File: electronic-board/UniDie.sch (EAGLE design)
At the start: 24 parts, among them IC1 ATMEGA88-THIN

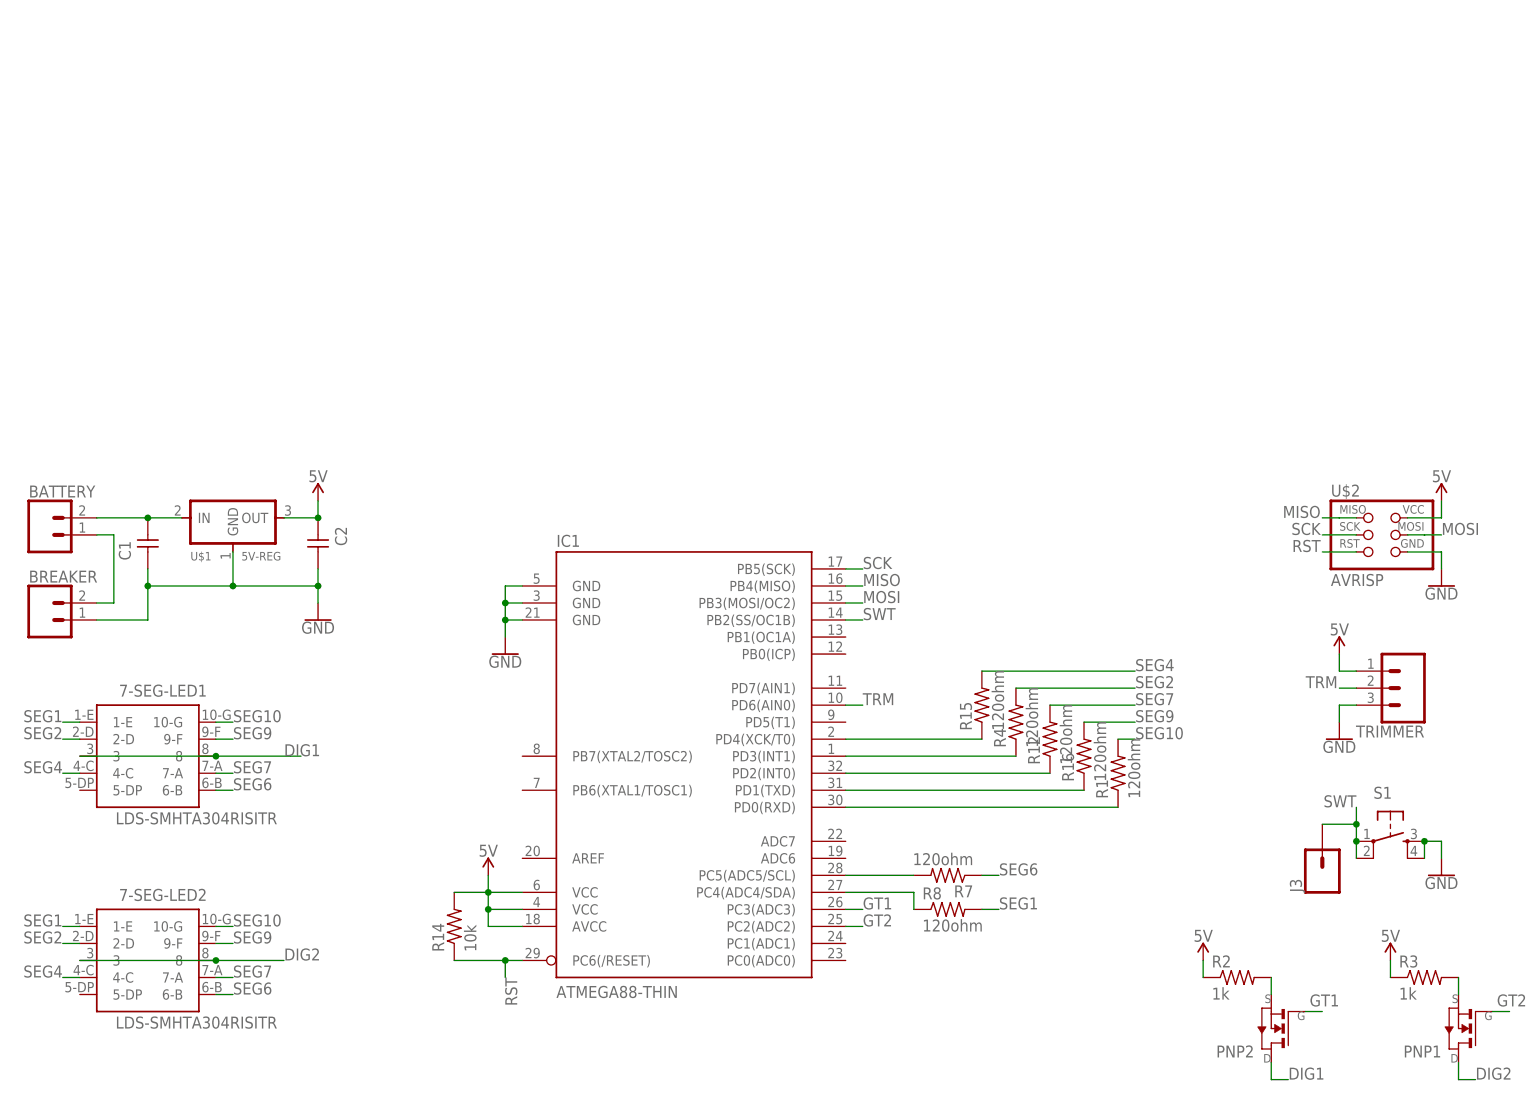
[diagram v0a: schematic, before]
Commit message: Design schematics for new controller
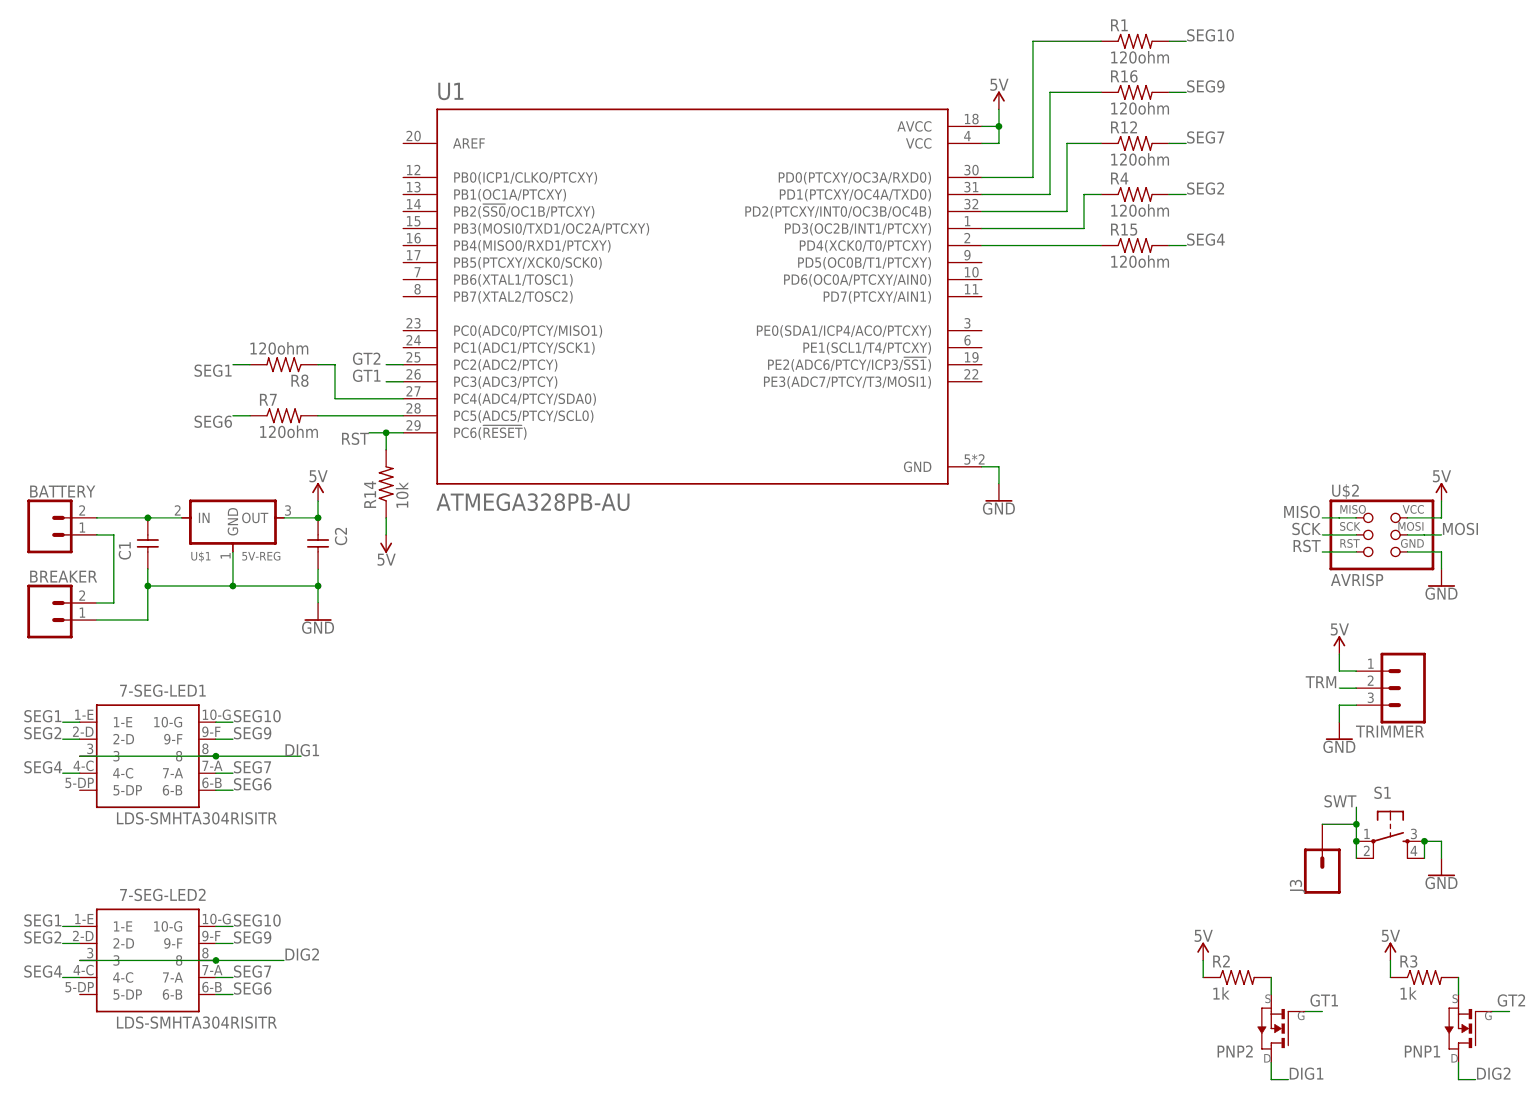
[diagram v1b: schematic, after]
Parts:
- removed IC1: ATMEGA88-THIN, fab:ATMEGA88-THIN
- added U1: ATMEGA328PB-AU, ATMEGA328PB-AU:ATMEGA328PB-AU
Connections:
- net 5V: now also R14.1, U1.AVCC, U1.VCC; no longer IC1.AVCC, IC1.VCC@1, IC1.VCC@2, R14.2
- net GND: now also U1.GND; no longer IC1.GND, IC1.GND@1, IC1.GND@2
- net GT1: now also U1.PC3(ADC3/PTCY); no longer IC1.PC3(ADC3)
- net GT2: now also U1.PC2(ADC2/PTCY); no longer IC1.PC2(ADC2)
- net MISO: no longer IC1.PB4(MISO)
- net MOSI: no longer IC1.PB3(MOSI/OC2)
- net N$10: now also U1.PD0(PTCXY/OC3A/RXD0); no longer IC1.PD0(RXD)
- net N$3: now also U1.PC5(ADC5/PTCY/SCL0); no longer IC1.PC5(ADC5/SCL)
- net N$4: now also U1.PC4(ADC4/PTCY/SDA0); no longer IC1.PC4(ADC4/SDA)
- net N$6: now also U1.PD4(XCK0/T0/PTCXY); no longer IC1.PD4(XCK/T0)
- net N$7: now also U1.PD3(OC2B/INT1/PTCXY); no longer IC1.PD3(INT1)
- net N$8: now also U1.PD2(PTCXY/INT0/OC3B/OC4B); no longer IC1.PD2(INT0)
- net N$9: now also U1.PD1(PTCXY/OC4A/TXD0); no longer IC1.PD1(TXD)
- net RST: now also R14.2, U1.PC6(!RESET!); no longer IC1.PC6(/RESET), R14.1
- net SCK: no longer IC1.PB5(SCK)
- net SWT: no longer IC1.PB2(SS/OC1B)
- net TRM: no longer IC1.PD6(AIN0)
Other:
- moved on the sheet: R1, R12, R14, R15, R16, R4, R7, R8

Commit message: Add thinner traces package for the microcontroller, re-arrange routes. To be finishes
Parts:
- removed U1: ATMEGA328PB-AU, ATMEGA328PB-AU:ATMEGA328PB-AU
- added U$3: ATMEGA328PB-AU-THIN, AG:ATMEGA328PB-AU-THIN
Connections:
- net 5V: now also U$3.AVCC, U$3.VCC; no longer U1.AVCC, U1.VCC
- net GND: now also U$3.GND, U$3.GND@1; no longer U1.GND
- net GT1: now also U$3.PC3(ADC3/PTCY); no longer U1.PC3(ADC3/PTCY)
- net GT2: now also U$3.PC2(ADC2/PTCY); no longer U1.PC2(ADC2/PTCY)
- net MISO: now also U$3.PC0(ADC0/PTCY/MISO1)
- net MOSI: now also U$3.PE3(ADC7/PTCY/T3/MOSI1)
- net N$10: now also U$3.PD0(PTCXY/OC3A/RXD0); no longer U1.PD0(PTCXY/OC3A/RXD0)
- net N$3: now also U$3.PC5(ADC5/PTCY/SCL0); no longer U1.PC5(ADC5/PTCY/SCL0)
- net N$4: now also U$3.PC4(ADC4/PTCY/SDA0); no longer U1.PC4(ADC4/PTCY/SDA0)
- net N$6: now also U$3.PD4(XCK0/T0/PTCXY); no longer U1.PD4(XCK0/T0/PTCXY)
- net N$7: now also U$3.PD3(OC2B/INT1/PTCXY); no longer U1.PD3(OC2B/INT1/PTCXY)
- net N$8: now also U$3.PD2(PTCXY/INT0/OC3B/OC4B); no longer U1.PD2(PTCXY/INT0/OC3B/OC4B)
- net N$9: now also U$3.PD1(PTCXY/OC4A/TXD0); no longer U1.PD1(PTCXY/OC4A/TXD0)
- net RST: now also U$3.PC6(!RESET!); no longer U1.PC6(!RESET!)
- net SCK: now also U$3.PC1(ADC1/PTCY/SCK1)

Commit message: Adjust all routes. Adjust trimmer holes. Adjust outline
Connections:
- net SWT: now also U$3.PB2(!SS0!/OC1B/PTCXY)
- net TRM: now also U$3.PD6(OC0A/PTCXY/AIN0)
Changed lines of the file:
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@@
 <grid distance="0.1" unitdist="inch" unit="inch" style="lines" multiple="1" display="no" altdistance="0.01" altunitdist="inch" altunit="inch"/>
 <layers>
-<layer number="1" name="Top" color="4" fill="1" visible="yes" active="no"/>
-<layer number="16" name="Bottom" color="1" fill="1" visible="yes" active="no"/>
-<layer number="17" name="Pads" color="2" fill="1" visible="yes" active="no"/>
-<layer number="18" name="Vias" color="2" fill="1" visible="yes" active="no"/>
-<layer number="19" name="Unrouted" color="6" fill="1" visible="yes" active="no"/>
-<layer number="20" name="Dimension" color="24" fill="1" visible="yes" active="no"/>
-<layer number="21" name="tPlace" color="7" fill="1" visible="yes" active="no"/>
-<layer number="22" name="bPlace" color="7" fill="1" visible="yes" active="no"/>
-<layer number="23" name="tOrigins" color="15" fill="1" visible="yes" active="no"/>
-<layer number="24" name="bOrigins" color="15" fill="1" visible="yes" active="no"/>
-<layer number="25" name="tNames" color="7" fill="1" visible="yes" active="no"/>
-<layer number="26" name="bNames" color="7" fill="1" visible="yes" active="no"/>
-<layer number="27" name="tValues" color="7" fill="1" visible="yes" active="no"/>
-<layer number="28" name="bValues" color="7" fill="1" visible="yes" active="no"/>
+<layer number="1" name="Top" color="4" fill="1" visible="no" active="no"/>
+<layer number="16" name="Bottom" color="1" fill="1" visible="no" active="no"/>
+<layer number="17" name="Pads" color="2" fill="1" visible="no" active="no"/>
+<layer number="18" name="Vias" color="2" fill="1" visible="no" active="no"/>
+<layer number="19" name="Unrouted" color="6" fill="1" visible="no" active="no"/>
+<layer number="20" name="Dimension" color="24" fill="1" visible="no" active="no"/>
+<layer number="21" name="tPlace" color="7" fill="1" visible="no" active="no"/>
+<layer number="22" name="bPlace" color="7" fill="1" visible="no" active="no"/>
+<layer number="23" name="tOrigins" color="15" fill="1" visible="no" active="no"/>
+<layer number="24" name="bOrigins" color="15" fill="1" visible="no" active="no"/>
+<layer number="25" name="tNames" color="7" fill="1" visible="no" active="no"/>
+<layer number="26" name="bNames" color="7" fill="1" visible="no" active="no"/>
+<layer number="27" name="tValues" color="7" fill="1" visible="no" active="no"/>
+<layer number="28" name="bValues" color="7" fill="1" visible="no" active="no"/>
 <layer number="29" name="tStop" color="7" fill="3" visible="no" active="no"/>
 <layer number="30" name="bStop" color="7" fill="6" visible="no" active="no"/>
@@
 <layer number="35" name="tGlue" color="7" fill="4" visible="no" active="no"/>
 <layer number="36" name="bGlue" color="7" fill="5" visible="no" active="no"/>
-<layer number="37" name="tTest" color="7" fill="1" visible="yes" active="no"/>
-<layer number="38" name="bTest" color="7" fill="1" visible="yes" active="no"/>
+<layer number="37" name="tTest" color="7" fill="1" visible="no" active="no"/>
+<layer number="38" name="bTest" color="7" fill="1" visible="no" active="no"/>
 <layer number="39" name="tKeepout" color="4" fill="11" visible="no" active="no"/>
 <layer number="40" name="bKeepout" color="1" fill="11" visible="no" active="no"/>
@@
 <layer number="44" name="Drills" color="7" fill="1" visible="no" active="no"/>
 <layer number="45" name="Holes" color="7" fill="1" visible="no" active="no"/>
-<layer number="46" name="Milling" color="3" fill="1" visible="yes" active="no"/>
-<layer number="47" name="Measures" color="7" fill="1" visible="yes" active="no"/>
-<layer number="48" name="Document" color="7" fill="1" visible="yes" active="no"/>
-<layer number="49" name="Reference" color="30" fill="1" visible="yes" active="no"/>
-<layer number="50" name="dxf" color="7" fill="1" visible="yes" active="no"/>
-<layer number="51" name="tDocu" color="7" fill="1" visible="yes" active="no"/>
-<layer number="52" name="bDocu" color="7" fill="1" visible="yes" active="no"/>
-<layer number="53" name="tGND_GNDA" color="7" fill="9" visible="yes" active="no"/>
-<layer number="54" name="bGND_GNDA" color="1" fill="9" visible="yes" active="no"/>
-<layer number="56" name="wert" color="7" fill="1" visible="yes" active="no"/>
-<layer number="57" name="tCAD" color="7" fill="1" visible="yes" active="no"/>
-<layer number="59" name="tCarbon" color="7" fill="1" visible="yes" active="no"/>
-<layer number="60" name="bCarbon" color="7" fill="1" visible="yes" active="no"/>
+<layer number="46" name="Milling" color="3" fill="1" visible="no" active="no"/>
+<layer number="47" name="Measures" color="7" fill="1" visible="no" active="no"/>
+<layer number="48" name="Document" color="7" fill="1" visible="no" active="no"/>
+<layer number="49" name="Reference" color="30" fill="1" visible="no" active="no"/>
+<layer number="50" name="dxf" color="7" fill="1" visible="no" active="no"/>
+<layer number="51" name="tDocu" color="7" fill="1" visible="no" active="no"/>
+<layer number="52" name="bDocu" color="7" fill="1" visible="no" active="no"/>
+<layer number="53" name="tGND_GNDA" color="7" fill="9" visible="no" active="no"/>
+<layer number="54" name="bGND_GNDA" color="1" fill="9" visible="no" active="no"/>
+<layer number="56" name="wert" color="7" fill="1" visible="no" active="no"/>
+<layer number="57" name="tCAD" color="7" fill="1" visible="no" active="no"/>
+<layer number="59" name="tCarbon" color="7" fill="1" visible="no" active="no"/>
+<layer number="60" name="bCarbon" color="7" fill="1" visible="no" active="no"/>
 <layer number="88" name="SimResults" color="9" fill="1" visible="yes" active="yes"/>
 <layer number="89" name="SimProbes" color="9" fill="1" visible="yes" active="yes"/>
@@
 <label x="220.726" y="47.498" size="1.778" layer="95" rot="R180"/>
 </segment>
+<segment>
+<pinref part="U$3" gate="G$1" pin="PD6(OC0A/PTCXY/AIN0)"/>
+<wire x1="167.64" y1="106.68" x2="170.18" y2="106.68" width="0.1524" layer="91"/>
+<label x="170.18" y="106.68" size="1.778" layer="95"/>
+</segment>
 </net>
 <net name="SWT" class="0">
@@
 <junction x="223.52" y="25.4"/>
 </segment>
-</net>
+<segment>
+<pinref part="U$3" gate="G$1" pin="PB2(!SS0!/OC1B/PTCXY)"/>
+<wire x1="81.28" y1="116.84" x2="78.74" y2="116.84" width="0.1524" layer="91"/>
+<label x="73.66" y="116.84" size="1.778" layer="95"/>
+</segment>
+</net>
